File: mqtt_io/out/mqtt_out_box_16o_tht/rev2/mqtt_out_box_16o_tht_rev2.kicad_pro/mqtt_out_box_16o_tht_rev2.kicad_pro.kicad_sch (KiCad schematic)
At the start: 143 parts, among them J1 Conn_01x04_Pin, J18 Conn_01x04_Pin, Q1 IRFZ24N, SW1 SW_DIP_x03, U1 MCP23017_SP

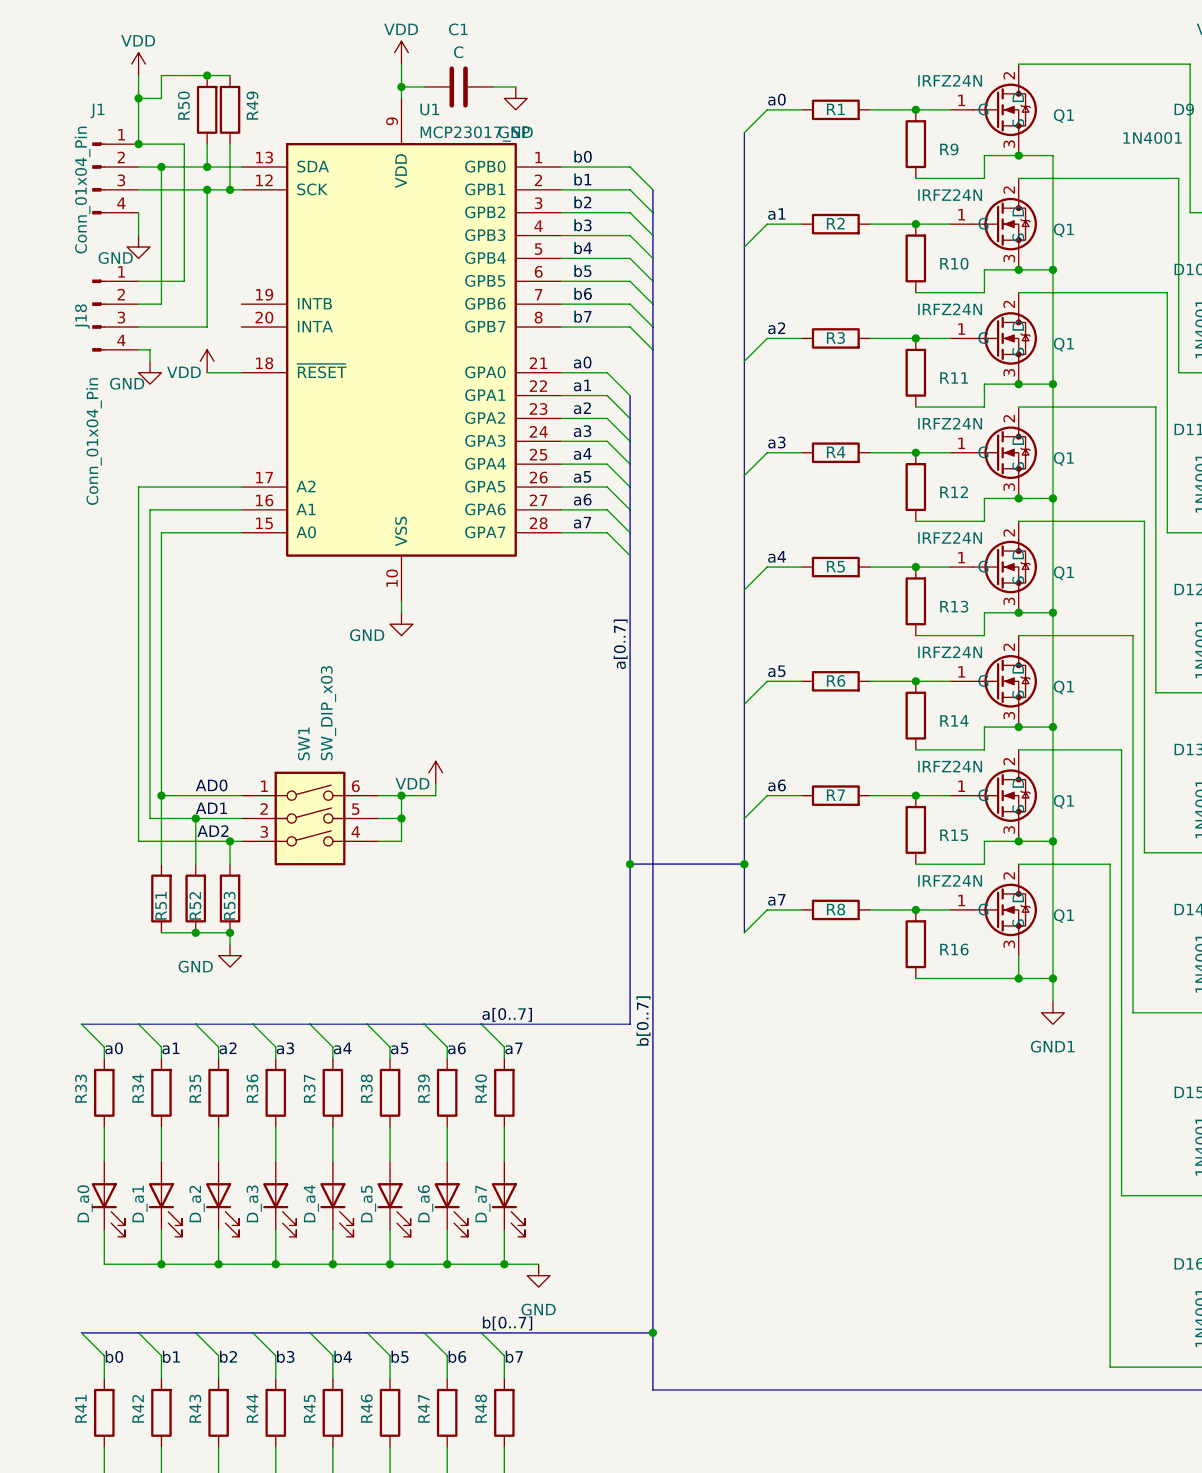
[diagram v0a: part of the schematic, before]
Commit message: Kleine Korrekturen
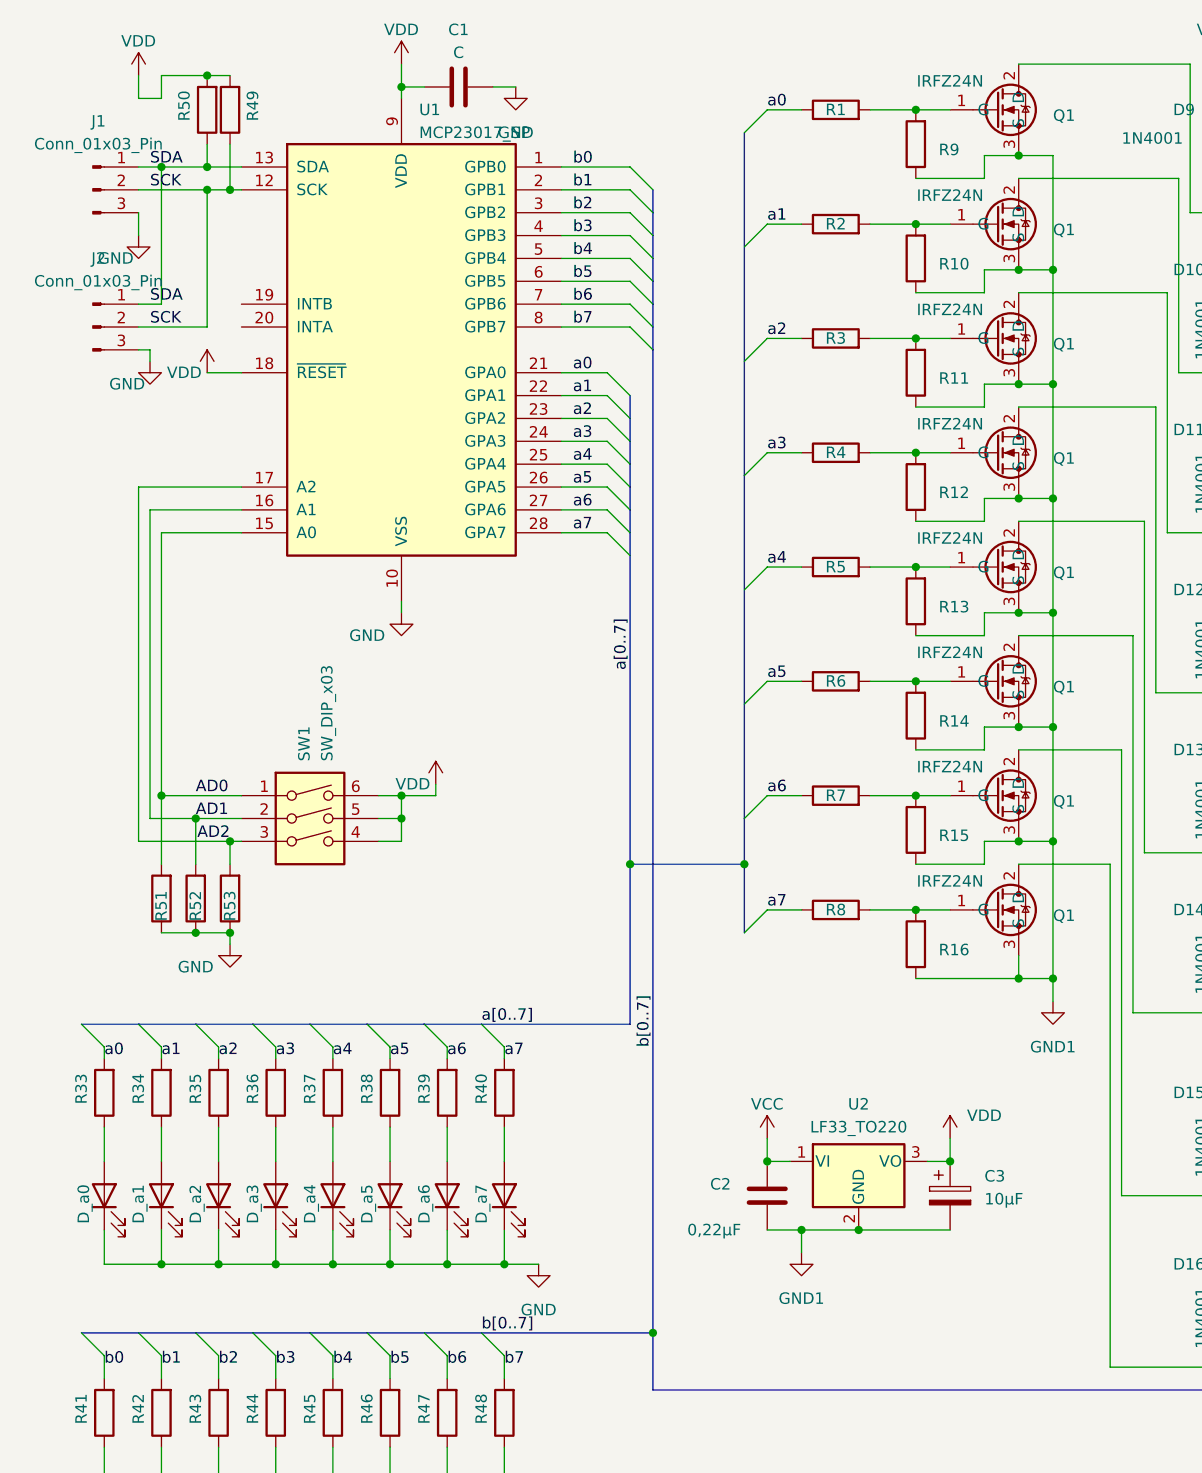
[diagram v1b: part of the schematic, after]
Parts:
- removed J1, J18: Conn_01x04_Pin, Connector_PinHeader_2.54mm:PinHeader_1x04_P2.54mm_Vertical, symbol Connector:Conn_01x04_Pin
- added C2: 0,22µF, Capacitor_THT:C_Disc_D5.0mm_W2.5mm_P5.00mm, symbol Device:C
- added C3: 10µF, Capacitor_THT:CP_Radial_D4.0mm_P2.00mm, symbol Device:C_Polarized
- added J1, J2: Conn_01x03_Pin, Connector_PinHeader_2.54mm:PinHeader_1x03_P2.54mm_Vertical, symbol Connector:Conn_01x03_Pin
- added U2: LF33_TO220, Package_TO_SOT_THT:TO-220-3_Vertical, symbol Regulator_Linear:LF33_TO220
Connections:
- net GND: now also C2.2, C3.2, J1.3 (Pin_3), J2.3 (Pin_3), U2.2 (GND)
- net VCC: now also C2.1, U2.1 (VI)
- net VDD: now also C3.1, U2.3 (VO)
- net SCK: now reaches R49.1, U1.12 (SCK)
- net SCK: now also J1.2 (Pin_2), J2.2 (Pin_2)
- net SDA: now reaches R50.1, U1.13 (SDA)
- net SDA: now also J1.1 (Pin_1), J2.1 (Pin_1)

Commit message: kleine Anpassungen
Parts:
- removed Q1 (x16): IRFZ24N, Package_TO_SOT_THT:TO-220-3_Vertical, symbol parts_tma_1:IRFZ_24N
- added Q1, Q10, Q11, Q12, Q13, Q14, Q15, Q16, Q2, Q3, Q4, Q5, Q6, Q7, Q8, Q9: 2N7000, Package_TO_SOT_THT:TO-92_Wide, symbol Transistor_FET:2N7000
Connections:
- net GND: now also Q1.1 (S), Q10.1 (S), Q11.1 (S), Q12.1 (S), Q13.1 (S), Q14.1 (S), Q15.1 (S), Q16.1 (S), Q2.1 (S), Q3.1 (S), Q4.1 (S), Q5.1 (S), Q6.1 (S), Q7.1 (S), Q8.1 (S), Q9.1 (S)
- net at R17.2, R25.2: now also Q9.2 (G)
- net at D1.2 (A), K_b0.A2: now also Q9.3 (D)
- net at D12.2 (A), K_a3.A2: now also Q4.3 (D)
- net at R15.2, R7.2: now also Q7.2 (G)
- net at D15.2 (A), K_a6.A2: now also Q7.3 (D)
- net at R19.2, R27.2: now also Q11.2 (G)
- net at R24.2, R32.2: now also Q16.2 (G)
- net at R18.2, R26.2: now also Q10.2 (G)
- net at D2.2 (A), K_b1.A2: now also Q10.3 (D)
- net at D5.2 (A), K_b4.A2: now also Q13.3 (D)
- net at R10.2, R2.2: now also Q2.2 (G)
- net at D10.2 (A), K_a1.A2: now also Q2.3 (D)
- net at D13.2 (A), K_a4.A2: now also Q5.3 (D)
- net at D3.2 (A), K_b2.A2: now also Q11.3 (D)
- net at R12.2, R4.2: now also Q4.2 (G)
- net at R14.2, R6.2: now also Q6.2 (G)
- net at D14.2 (A), K_a5.A2: now also Q6.3 (D)
- net at R13.2, R5.2: now also Q5.2 (G)
- net at D7.2 (A), K_b6.A2: now also Q15.3 (D)
- net at D6.2 (A), K_b5.A2: now also Q14.3 (D)
- net at R22.2, R30.2: now also Q14.2 (G)
- net at R20.2, R28.2: now also Q12.2 (G)
- net at D9.2 (A), K_a0.A2: now also Q1.3 (D)
- net at R16.2, R8.2: now also Q8.2 (G)
- net at R11.2, R3.2: now also Q3.2 (G)
- net at D4.2 (A), K_b3.A2: now also Q12.3 (D)
- net at D16.2 (A), K_a7.A2: now also Q8.3 (D)
- net at D8.2 (A), K_b7.A2: now also Q16.3 (D)
- net at R1.2, R9.2: now also Q1.2 (G)
- net at R21.2, R29.2: now also Q13.2 (G)
- net at R23.2, R31.2: now also Q15.2 (G)
- net at D11.2 (A), K_a2.A2: now also Q3.3 (D)

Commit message: kleine Korrekturen
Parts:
- C1: value C -> 100n
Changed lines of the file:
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@@
       (effects (font (size 1.27 1.27)))
     )
-    (property "Value" "C" (at 55.88 15.24 90)
+    (property "Value" "100n" (at 55.88 15.24 90)
       (effects (font (size 1.27 1.27)))
     )

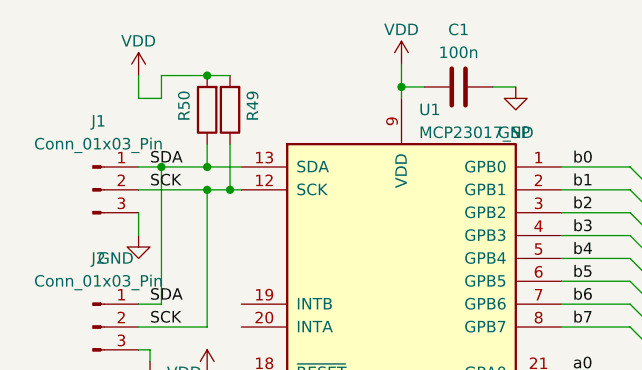
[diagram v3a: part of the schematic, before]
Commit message: Jumper, Beschriftung
Jumper für pullupWiderstände bei SDA und SCK eingefügt. Die Widerstände
sind nun zuschaltbar.
Beschriftung für in SDA/SCK/GND und Spannungsversorgung angebracht.
PDFs neu generiert.
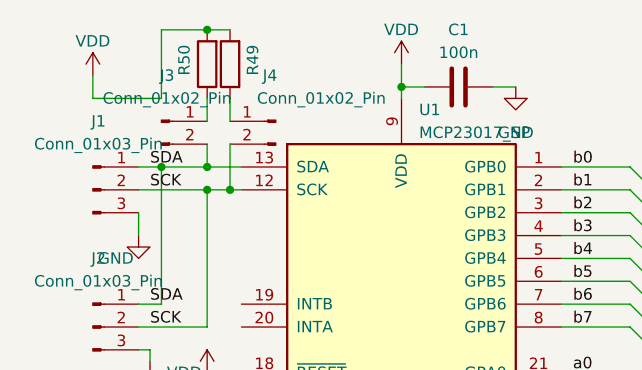
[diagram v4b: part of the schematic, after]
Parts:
- added J3, J4: Conn_01x02_Pin, Connector_PinHeader_2.54mm:PinHeader_1x02_P2.54mm_Vertical, symbol Connector:Conn_01x02_Pin
- R33: value 330R -> (510/330R)
- R41: value 330R -> 330R(750)
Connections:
- net SCK: now also J4.2 (Pin_2); no longer R49.1
- net SDA: now also J3.2 (Pin_2); no longer R50.1
- new net: J4.1 (Pin_1), R49.1
- new net: J3.1 (Pin_1), R50.1
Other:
- moved on the sheet: R49, R50
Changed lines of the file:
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@@
   (junction (at 238.76 71.12) (diameter 0) (color 0 0 0 0)
   )
-  (junction (at 27.94 27.94) (diameter 0) (color 0 0 0 0)
-  )
   (junction (at 140.97 88.9) (diameter 0) (color 0 0 0 0)
   )
@@
   (junction (at 204.47 46.99) (diameter 0) (color 0 0 0 0)
   )
-  (junction (at 27.94 17.78) (diameter 0) (color 0 0 0 0)
-  )
   (junction (at 30.48 30.48) (diameter 0) (color 0 0 0 0)
   )
+  (junction (at 27.94 12.7) (diameter 0) (color 0 0 0 0)
+  )
   (junction (at 139.7 53.34) (diameter 0) (color 0 0 0 0)
   )
@@
   (junction (at 238.76 88.9) (diameter 0) (color 0 0 0 0)
   )
+  (junction (at 27.94 27.94) (diameter 0) (color 0 0 0 0)
+  )
   (junction (at 121.92 90.17) (diameter 0) (color 0 0 0 0)
   )
@@
     (stroke (width 0) (type default))
   )
-  (wire (pts (xy 22.86 17.78) (xy 22.86 20.32))
+  (wire (pts (xy 22.86 12.7) (xy 22.86 20.32))
     (stroke (width 0) (type default))
   )
@@
     (stroke (width 0) (type default))
   )
+  (wire (pts (xy 30.48 25.4) (xy 30.48 30.48))
+    (stroke (width 0) (type default))
+  )
   (wire (pts (xy 237.49 53.34) (xy 237.49 71.12))
     (stroke (width 0) (type default))
@@
     (stroke (width 0) (type default))
   )
+  (wire (pts (xy 27.94 27.94) (xy 31.75 27.94))
+    (stroke (width 0) (type default))
+  )
   (bus (pts (xy 77.47 33.02) (xy 77.47 35.56))
     (stroke (width 0) (type default))
@@
     (stroke (width 0) (type default))
   )
-  (wire (pts (xy 22.86 27.94) (xy 27.94 27.94))
-    (stroke (width 0) (type default))
-  )
   (wire (pts (xy 106.68 46.99) (xy 110.49 46.99))
     (stroke (width 0) (type default))
@@
     (stroke (width 0) (type default))
   )
-  (wire (pts (xy 20.32 17.78) (xy 20.32 20.32))
+  (wire (pts (xy 15.24 17.78) (xy 15.24 20.32))
     (stroke (width 0) (type default))
   )
@@
     (stroke (width 0) (type default))
   )
-  (wire (pts (xy 22.86 20.32) (xy 20.32 20.32))
+  (wire (pts (xy 22.86 20.32) (xy 15.24 20.32))
     (stroke (width 0) (type default))
   )
@@
     (stroke (width 0) (type default))
   )
-  (wire (pts (xy 27.94 30.48) (xy 30.48 30.48))
-    (stroke (width 0) (type default))
-  )
   (bus (pts (xy 45.72 123.19) (xy 52.07 123.19))
     (stroke (width 0) (type default))
@@
     (stroke (width 0) (type default))
   )
-  (wire (pts (xy 30.48 30.48) (xy 31.75 30.48))
+  (wire (pts (xy 27.94 30.48) (xy 30.48 30.48))
     (stroke (width 0) (type default))
   )
@@
     (stroke (width 0) (type default))
   )
+  (wire (pts (xy 30.48 20.32) (xy 30.48 22.86))
+    (stroke (width 0) (type default))
+  )
   (wire (pts (xy 140.97 68.58) (xy 149.86 68.58))
     (stroke (width 0) (type default))
@@
     (stroke (width 0) (type default))
   )
-  (wire (pts (xy 22.86 17.78) (xy 27.94 17.78))
+  (wire (pts (xy 22.86 12.7) (xy 27.94 12.7))
     (stroke (width 0) (type default))
   )
@@
     (stroke (width 0) (type default))
   )
+  (wire (pts (xy 27.94 20.32) (xy 27.94 22.86))
+    (stroke (width 0) (type default))
+  )
   (wire (pts (xy 162.56 35.56) (xy 173.99 35.56))
     (stroke (width 0) (type default))
@@
     (stroke (width 0) (type default))
   )
-  (wire (pts (xy 27.94 27.94) (xy 31.75 27.94))
+  (wire (pts (xy 22.86 27.94) (xy 27.94 27.94))
     (stroke (width 0) (type default))
   )
@@
     (stroke (width 0) (type default))
   )
-  (wire (pts (xy 27.94 25.4) (xy 27.94 27.94))
-    (stroke (width 0) (type default))
-  )
   (bus (pts (xy 77.47 45.72) (xy 77.47 48.26))
     (stroke (width 0) (type default))
@@
     (stroke (width 0) (type default))
   )
-  (wire (pts (xy 27.94 17.78) (xy 30.48 17.78))
+  (wire (pts (xy 27.94 12.7) (xy 30.48 12.7))
     (stroke (width 0) (type default))
   )
@@
     (stroke (width 0) (type default))
   )
-  (wire (pts (xy 30.48 25.4) (xy 30.48 30.48))
-    (stroke (width 0) (type default))
-  )
   (wire (pts (xy 54.61 160.02) (xy 54.61 162.56))
     (stroke (width 0) (type default))
@@
     (stroke (width 0) (type default))
   )
+  (wire (pts (xy 27.94 25.4) (xy 27.94 27.94))
+    (stroke (width 0) (type default))
+  )
   (wire (pts (xy 269.24 25.4) (xy 269.24 16.51))
     (stroke (width 0) (type default))
@@
     (stroke (width 0) (type default))
   )
+  (wire (pts (xy 30.48 30.48) (xy 31.75 30.48))
+    (stroke (width 0) (type default))
+  )
   (wire (pts (xy 53.34 97.79) (xy 53.34 96.52))
     (stroke (width 0) (type default))
@@
       (effects (font (size 1.27 1.27)) (justify right))
     )
-    (property "Value" "330R" (at 13.97 166.37 90)
+    (property "Value" "330R(750)" (at 13.97 166.37 90)
       (effects (font (size 1.27 1.27)) hide)
     )
@@
     )
   )
-  (symbol (lib_id "power:VDD") (at 20.32 17.78 0) (unit 1)
+  (symbol (lib_id "power:VDD") (at 15.24 17.78 0) (unit 1)
     (in_bom yes) (on_board yes) (dnp no) (fields_autoplaced)
-    (property "Reference" "#PWR05" (at 20.32 21.59 0)
+    (property "Reference" "#PWR05" (at 15.24 21.59 0)
       (effects (font (size 1.27 1.27)) hide)
     )
-    (property "Value" "VDD" (at 20.32 13.97 0)
+    (property "Value" "VDD" (at 15.24 13.97 0)
       (effects (font (size 1.27 1.27)))
     )
-    (property "Footprint" "" (at 20.32 17.78 0)
+    (property "Footprint" "" (at 15.24 17.78 0)
       (effects (font (size 1.27 1.27)) hide)
     )
-    (property "Datasheet" "" (at 20.32 17.78 0)
+    (property "Datasheet" "" (at 15.24 17.78 0)
       (effects (font (size 1.27 1.27)) hide)
     )
@@
     )
   )
+  (symbol (lib_id "Connector:Conn_01x02_Pin") (at 35.56 22.86 0) (mirror y) (unit 1)
+    (in_bom yes) (on_board yes) (dnp no)
+    (property "Reference" "J4" (at 34.925 17.78 0)
+      (effects (font (size 1.27 1.27)))
+    )
+    (property "Value" "Conn_01x02_Pin" (at 40.64 20.32 0)
+      (effects (font (size 1.27 1.27)))
+    )
+    (property "Footprint" "Connector_PinHeader_2.54mm:PinHeader_1x02_P2.54mm_Vertical" (at 35.56 22.86 0)
+      (effects (font (size 1.27 1.27)) hide)
+    )
+    (property "Datasheet" "~" (at 35.56 22.86 0)
+      (effects (font (size 1.27 1.27)) hide)
+    )
+    (pin "1")
+    (pin "2")
+    (instances
+      (project "mqtt_out_box_16o_tht_rev2.kicad_pro"
+        (path "/c627dcd6-05c4-47a7-af36-f14e587162a0"
+          (reference "J4") (unit 1)
+        )
+      )
+    )
+  )
   (symbol (lib_id "Transistor_FET:2N7000") (at 115.57 110.49 0) (unit 1)
     (in_bom yes) (on_board yes) (dnp no) (fields_autoplaced)
@@
     )
   )
-  (symbol (lib_id "Device:R") (at 30.48 21.59 180) (unit 1)
+  (symbol (lib_id "Device:R") (at 30.48 16.51 180) (unit 1)
     (in_bom yes) (on_board yes) (dnp no)
-    (property "Reference" "R49" (at 33.02 22.86 90)
+    (property "Reference" "R49" (at 33.02 17.78 90)
       (effects (font (size 1.27 1.27)) (justify right))
     )
-    (property "Value" "4k7" (at 27.94 21.59 90)
+    (property "Value" "4k7" (at 27.94 16.51 90)
       (effects (font (size 1.27 1.27)) hide)
     )
-    (property "Footprint" "Resistor_THT:R_Axial_DIN0204_L3.6mm_D1.6mm_P7.62mm_Horizontal" (at 32.258 21.59 90)
+    (property "Footprint" "Resistor_THT:R_Axial_DIN0204_L3.6mm_D1.6mm_P7.62mm_Horizontal" (at 32.258 16.51 90)
       (effects (font (size 1.27 1.27)) hide)
     )
-    (property "Datasheet" "~" (at 30.48 21.59 0)
+    (property "Datasheet" "~" (at 30.48 16.51 0)
       (effects (font (size 1.27 1.27)) hide)
     )
@@
     )
   )
-  (symbol (lib_id "Device:R") (at 27.94 21.59 180) (unit 1)
+  (symbol (lib_id "Device:R") (at 27.94 16.51 180) (unit 1)
     (in_bom yes) (on_board yes) (dnp no)
-    (property "Reference" "R50" (at 25.4 22.86 90)
+    (property "Reference" "R50" (at 25.4 17.78 90)
       (effects (font (size 1.27 1.27)) (justify right))
     )
-    (property "Value" "4k7" (at 25.4 21.59 90)
+    (property "Value" "4k7" (at 25.4 16.51 90)
       (effects (font (size 1.27 1.27)) hide)
     )
-    (property "Footprint" "Resistor_THT:R_Axial_DIN0204_L3.6mm_D1.6mm_P7.62mm_Horizontal" (at 29.718 21.59 90)
+    (property "Footprint" "Resistor_THT:R_Axial_DIN0204_L3.6mm_D1.6mm_P7.62mm_Horizontal" (at 29.718 16.51 90)
       (effects (font (size 1.27 1.27)) hide)
     )
-    (property "Datasheet" "~" (at 27.94 21.59 0)
+    (property "Datasheet" "~" (at 27.94 16.51 0)
       (effects (font (size 1.27 1.27)) hide)
     )
@@
       (effects (font (size 1.27 1.27)) (justify right))
     )
-    (property "Value" "330R" (at 13.97 130.81 90)
+    (property "Value" " (510/330R)" (at 13.97 130.81 90)
       (effects (font (size 1.27 1.27)) hide)
     )
@@
         )
       )
+    )
+  )
+  (symbol (lib_id "Connector:Conn_01x02_Pin") (at 22.86 22.86 0) (unit 1)
+    (in_bom yes) (on_board yes) (dnp no) (fields_autoplaced)
+    (property "Reference" "J3" (at 23.495 17.78 0)
+      (effects (font (size 1.27 1.27)))
+    )
+    (property "Value" "Conn_01x02_Pin" (at 23.495 20.32 0)
+      (effects (font (size 1.27 1.27)))
+    )
+    (property "Footprint" "Connector_PinHeader_2.54mm:PinHeader_1x02_P2.54mm_Vertical" (at 22.86 22.86 0)
+      (effects (font (size 1.27 1.27)) hide)
+    )
+    (property "Datasheet" "~" (at 22.86 22.86 0)
+      (effects (font (size 1.27 1.27)) hide)
+    )
+    (pin "1")
+    (pin "2")
+    (instances
+      (project "mqtt_out_box_16o_tht_rev2.kicad_pro"
+        (path "/c627dcd6-05c4-47a7-af36-f14e587162a0"
+          (reference "J3") (unit 1)
+        )
+      )
